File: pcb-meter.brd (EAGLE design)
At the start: 100 x 80 mm, 41 parts

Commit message: Update
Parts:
- added C3, C5, C8, C9: 100n, capacitors:C050-024X044
- added C4, C6: 10u/35V, capacitors-electrolytic:E2-5
- added HL13: BLUE(3MM), optoelectronics:LED3MM-H
- added R20: 1.5k, resistors:R-0207/10
- moved R19 623.9 mm to (34.0, 30.0), turned to 270 degrees
- moved R18 616.2 mm to (43.5, 35.0), turned to 180 degrees
- moved R17 600.3 mm to (43.5, 32.5), turned to 180 degrees
- moved R16 584.3 mm to (43.5, 30.0), turned to 180 degrees
- moved R15 577.1 mm to (56.0, 35.0), turned to 180 degrees
- moved R14 561.2 mm to (56.0, 32.5), turned to 180 degrees
- moved R13 545.3 mm to (56.0, 30.0), turned to 180 degrees
- moved R12 538.5 mm to (68.5, 35.0), turned to 180 degrees
- moved R11 522.7 mm to (68.5, 32.5), turned to 180 degrees
- moved R10 506.9 mm to (68.5, 30.0), turned to 180 degrees
- moved R9 500.6 mm to (81.0, 35.0), turned to 180 degrees
- moved R8 482.4 mm to (81.0, 30.0), turned to 180 degrees
- moved R7 471.6 mm to (81.0, 32.5), turned to 180 degrees
- moved HL12 436.4 mm to (95.5, 6.00), flipped to the bottom, turned to 180 degrees
- moved HL11 419.7 mm to (90.5, 6.00), flipped to the bottom, turned to 180 degrees
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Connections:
- removed net V+: DA1.8, DA2.3, DA3.3, DA4.3
- removed net V-: DA1.4, DA2.12, DA3.12, DA4.12
- new net N$36: DA1.6, DA1.7
- net +15V: now also C3.2, C4.+, C5.2, C8.2, C9.2, DA1.8, DA2.3, DA3.3, DA4.3
- net -15V: now also C3.1, C5.1, C6.-, C8.1, C9.1, DA1.4, DA2.12, DA3.12, DA4.12
- net GND: now also C4.-, C6.+, DA1.5, HL13.K
- net N$1: now also R20.2
- net N$11: now also DA4.4; no longer DA4.10
- net N$12: now also DA4.6; no longer DA4.8
- net N$13: now also DA4.10; no longer DA4.6
- net N$14: now also DA4.2; no longer DA4.13
- net N$15: now also DA4.1; no longer DA4.14
- net N$16: now also DA4.13; no longer DA4.1
- net N$17: now also DA4.14; no longer DA4.2
- net N$18: now also DA3.2; no longer DA3.13
- net N$19: now also DA3.1; no longer DA3.14
- net N$2: now also R1.1
- net N$20: now also DA3.13; no longer DA3.1
- net N$21: now also DA3.14; no longer DA3.2
- net N$22: now also DA2.2; no longer DA2.13
- net N$23: now also DA2.1; no longer DA2.14
- net N$24: now also DA2.13; no longer DA2.1
- net N$25: now also DA2.14; no longer DA2.2
- net N$26: now also C1.+, R3.2
- net N$27: now also DA4.8; no longer DA4.4
- net N$28: now also DA3.4; no longer DA3.10
- net N$29: now also DA3.6; no longer DA3.8
- net N$30: now also DA3.10; no longer DA3.6
- net N$31: now also DA3.8; no longer DA3.4
- net N$32: now also DA2.4; no longer DA2.10
- net N$33: now also DA2.6; no longer DA2.8
- net N$34: now also DA2.10; no longer DA2.6
- net N$35: now also DA2.8; no longer DA2.4
- net N$9: now also HL13.A, R20.1; no longer C1.+, R3.2
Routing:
- net -15V: track 0.00 -> 152.0 mm
- net +15V: track 0.00 -> 128.1 mm
- net N$1: track 0.00 -> 94.1 mm
- net N$26: track 0.00 -> 90.6 mm
- net N$14: track 0.00 -> 28.3 mm
- net N$28: track 0.00 -> 25.3 mm
- net N$5: track 0.00 -> 24.9 mm
- net N$8: track 0.00 -> 24.4 mm
- net N$34: track 0.00 -> 23.0 mm
- net N$11: track 0.00 -> 22.4 mm
- net N$16: track 0.00 -> 22.0 mm
- net N$12: track 0.00 -> 21.2 mm
- net N$33: track 0.00 -> 20.2 mm
- net N$30: track 0.00 -> 20.2 mm
- net N$13: track 0.00 -> 19.9 mm
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- added copper zone on layer 1, net GND
- added copper zone on layer 16, net GND
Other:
- board size 100 x 80 mm -> 68.5 x 35 mm

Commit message: Renumber pcb-meter
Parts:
- removed C9: 100n, capacitors:C050-024X044
- added C7: 1u/50V, capacitors-electrolytic:E1,5-4
- C1: value 1u/50V -> 10u/35V; device capacitors-electrolytic:E1,5-4 -> capacitors-electrolytic:E2-5
- C2: value 47n -> 10u/35V; device capacitors:C050-025X075 -> capacitors-electrolytic:E2-5
- C4, C6: value 10u/35V -> 100n; device capacitors-electrolytic:E2-5 -> capacitors:C050-024X044
- C8: value 100n -> 47n; device capacitors:C050-024X044 -> capacitors:C050-025X075
- HL1: value GREEN(3MM) -> BLUE(3MM)
- HL12: value RED(3MM) -> YELLOW(3MM)
- HL13: value BLUE(3MM) -> RED(3MM)
- HL9: value YELLOW(3MM) -> GREEN(3MM)
- R1: value 56k -> 1.5k
- R10: value 2.2k -> 560R
- R11: value 1.5k -> 820R
- R13: value 820R -> 1.5k
- R14: value 560R -> 2.2k
- R15: value 330R -> 3.3k
- R16: value 330R -> 12k
- R17: value 220R -> 5.6k
- R18: value 220R -> 15k
- R19: value 270R -> 1k
- R2: value 150k -> 56k
- R20: value 1.5k -> 180R
- R3: value 1.8k -> 150k
- R4: value 15k -> 1.8k
- R5: value 180R -> 270R
- R6: value 1k -> 220R
- R7: value 12k -> 220R
- R8: value 5.6k -> 330R
- R9: value 3.3k -> 330R
- moved R1 65.0 mm to (31.5, 30.0)
- moved R4 63.0 mm to (97.0, 14.0), turned to 90 degrees
- moved HL13 62.5 mm to (95.5, 6.00)
- moved C2 53.2 mm to (90.0, 31.0)
- moved C6 49.4 mm to (46.0, 8.50), turned to 0 degrees
- moved C3 40.3 mm to (81.5, 27.5), turned to 180 degrees
- moved R16 37.6 mm to (81.0, 32.5)
- moved R17 37.6 mm to (81.0, 30.0)
- moved R7 37.5 mm to (43.5, 32.5)
- moved R8 37.5 mm to (43.5, 30.0)
- moved C4 34.0 mm to (70.0, 8.50), turned to 0 degrees
- moved C8 31.9 mm to (39.0, 16.0), turned to 90 degrees
- moved R15 25.0 mm to (81.0, 35.0)
- moved R9 25.0 mm to (56.0, 35.0)
- moved DA2 24.0 mm to (70.0, 19.5)
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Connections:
- net +15V: now also C1.+, C4.2, C6.2, R17.1, R19.2, R20.2; no longer C2.2, C4.+, C9.2, R5.2, R6.2, R8.1
- net -15V: now also C2.-, C4.1, C6.1, HL13.K, R18.1; no longer C6.-, C8.1, C9.1, HL12.K, R4.1
- net GND: now also C2.+, C7.-, HL1.K, R5.2; no longer C4.-, C6.+, HL13.K, R19.2
- net N$1: now also R1.2; no longer R20.2
- net N$10: now also C8.1, R20.1; no longer C2.1, R5.1
- net N$11: now also DA2.4, R16.1, R17.2; no longer DA4.4, R7.1, R8.2
- net N$12: now also DA2.6, R15.1, R16.2; no longer DA4.6, R7.2, R9.1
- net N$13: now also DA2.10, R14.1, R15.2; no longer DA4.10, R10.1, R9.2
- net N$14: now also DA2.2, HL12.K, HL13.A; no longer DA4.2, HL11.K, HL12.A
- net N$15: now also DA2.1, HL11.K, HL12.A; no longer DA4.1, HL10.K, HL11.A
- net N$16: now also DA2.13, HL10.K, HL11.A; no longer DA4.13, HL10.A, HL9.K
- net N$17: now also DA2.14, HL10.A, HL9.K; no longer DA4.14, HL8.K, HL9.A
- net N$18: now also DA4.2, HL8.K, HL9.A; no longer DA3.2, HL7.K, HL8.A
- net N$19: now also DA4.1, HL7.K, HL8.A; no longer DA3.1, HL6.K, HL7.A
- net N$2: now also R2.1; no longer R1.1
- net N$20: now also DA4.13, HL6.K, HL7.A; no longer DA3.13, HL5.K, HL6.A
- net N$21: now also DA4.14, HL5.K, HL6.A; no longer DA3.14, HL4.K, HL5.A
- net N$22: now also DA3.2, HL4.K, HL5.A; no longer DA2.2, HL3.K, HL4.A
- net N$23: now also DA3.1, HL3.K, HL4.A; no longer DA2.1, HL2.K, HL3.A
- net N$24: now also DA3.13, HL2.K, HL3.A; no longer DA2.13, HL1.K, HL2.A
- net N$25: now also DA3.14, HL2.A; no longer DA2.14, HL1.A
- net N$26: now also C7.+, R4.2; no longer C1.+, R3.2
- net N$27: now also DA2.8, R13.1, R14.2; no longer DA4.8, R10.2, R11.1
- net N$28: now also DA4.4, R13.2; no longer DA3.4, R11.2
- net N$29: now also DA4.6, R11.1; no longer DA3.6, R13.1
- net N$30: now also DA4.10, R10.1, R11.2; no longer DA3.10, R13.2, R14.1
- net N$31: now also DA4.8, R10.2, R9.1; no longer DA3.8, R14.2, R15.1
- net N$32: now also DA3.4, R8.1, R9.2; no longer DA2.4, R15.2, R16.1
- net N$33: now also DA3.6, R7.1, R8.2; no longer DA2.6, R16.2, R17.1
- net N$34: now also DA3.10, R6.1, R7.2; no longer DA2.10, R17.2, R18.1
- net N$35: now also DA3.8, R5.1, R6.2; no longer DA2.8, R18.2, R19.1
- net N$5: now also R2.2, R3.1; no longer R1.2, R2.1
- net N$6: now also R18.2, R19.1; no longer R4.2, R6.1
- net N$8: now also R3.2, R4.1; no longer R2.2, R3.1
- net N$9: now also HL1.A, R1.1; no longer HL13.A, R20.1

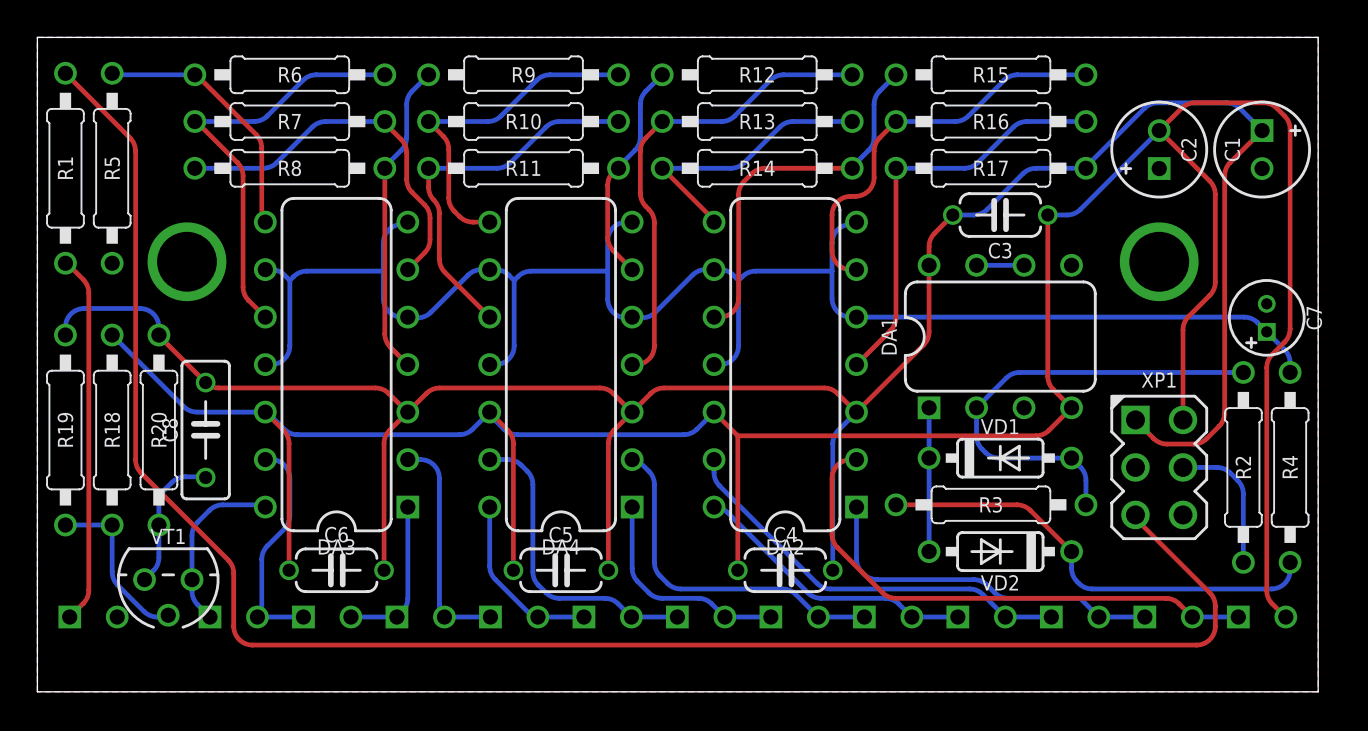
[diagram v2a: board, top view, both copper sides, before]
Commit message: Remove PP indicator
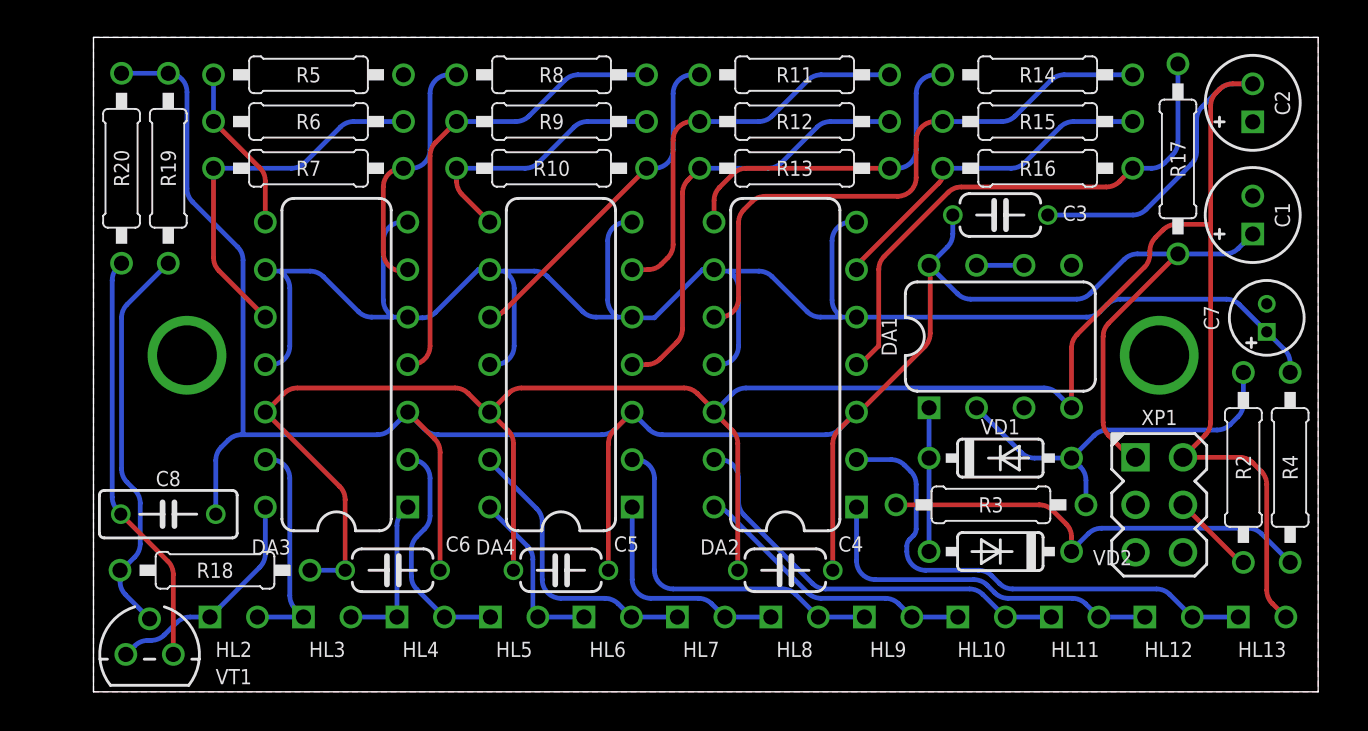
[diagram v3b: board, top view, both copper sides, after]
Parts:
- removed HL1: BLUE(3MM), optoelectronics:LED3MM-H
- removed R1: 1.5k, resistors:R-0207/10
- moved R14 15.8 mm to (83.5, 35.0)
- moved R11 15.3 mm to (70.5, 35.0)
- moved R19 15.0 mm to (37.0, 30.0)
- moved R8 14.9 mm to (57.5, 35.0)
- moved R20 14.1 mm to (34.5, 30.0)
- moved R5 11.6 mm to (44.5, 35.0), turned to 0 degrees
- moved R17 10.0 mm to (91.0, 30.5), turned to 90 degrees
- moved R18 9.30 mm to (39.5, 8.50), turned to 180 degrees
- moved C2 5.59 mm to (95.0, 33.5)
- moved C8 4.92 mm to (37.0, 11.5), turned to 0 degrees
- moved VT1 4.12 mm to (36.0, 4.00), turned to 0 degrees
- moved C1 3.54 mm to (95.0, 27.5), turned to 90 degrees
- moved R15 3.54 mm to (83.5, 32.5)
- moved R16 3.54 mm to (83.5, 30.0)
- moved R12 3.20 mm to (70.5, 32.5)
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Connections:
- removed net N$1: R1.2, XP1.5
- removed net N$9: HL1.A, R1.1
- net GND: no longer HL1.K
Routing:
- net N$1: track 94.1 -> 0.00 mm
- net N$9: track 19.8 -> 0.00 mm
- net N$10: track 7.56 -> 22.3 mm
- net -15V: track 152.0 -> 139.7 mm
- net N$6: track 9.16 -> 21.3 mm
- net N$13: track 19.9 -> 31.3 mm
- net N$29: track 12.0 -> 21.3 mm
- net N$32: track 16.8 -> 25.2 mm
- net +15V: track 128.1 -> 135.6 mm
- net N$26: track 90.6 -> 97.5 mm
- net N$33: track 20.2 -> 13.4 mm
- net N$11: track 22.4 -> 28.9 mm
- net N$35: track 13.9 -> 8.96 mm
- net N$5: track 24.9 -> 21.0 mm
- net N$31: track 18.4 -> 14.6 mm
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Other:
- board size 68.5 x 35 mm -> 65.5 x 35 mm

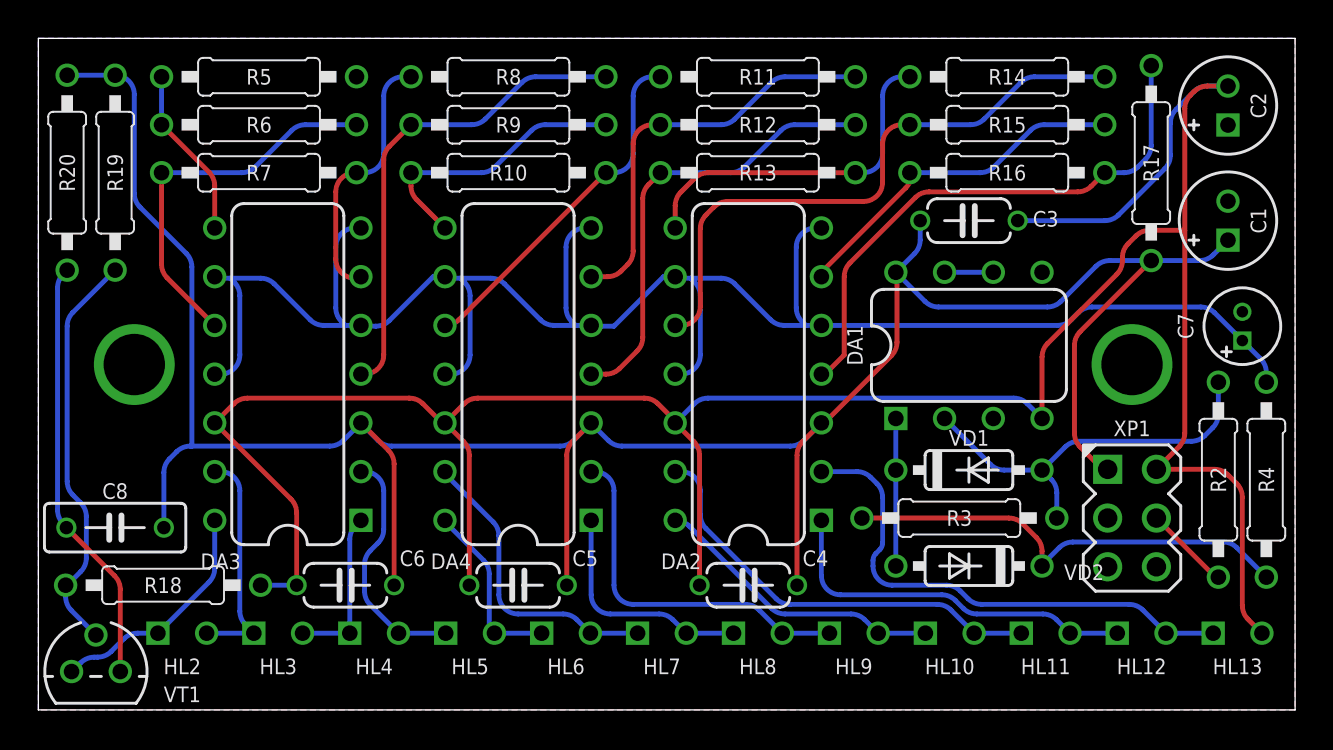
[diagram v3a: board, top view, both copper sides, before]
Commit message: Round pcb edges for pcb-meter
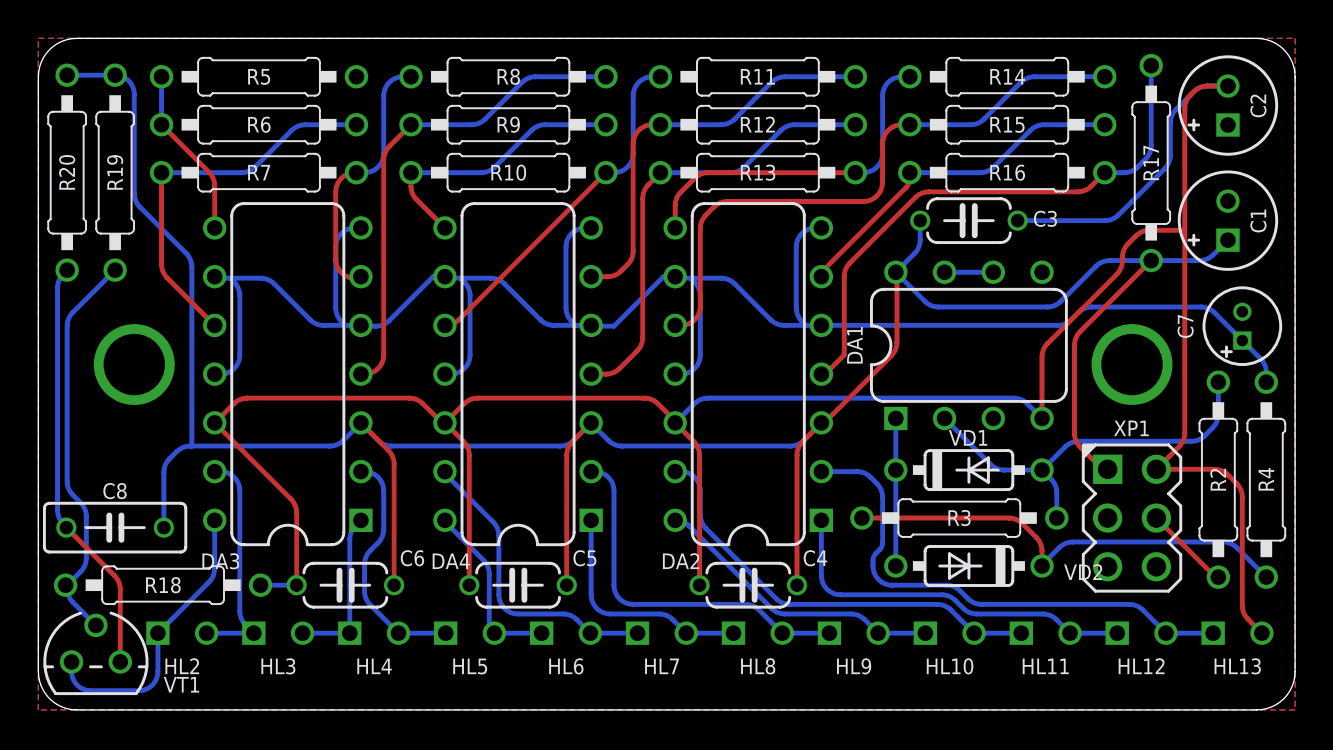
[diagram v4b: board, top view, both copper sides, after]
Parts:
- moved VT1 0.50 mm to (36.0, 4.50)
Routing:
- net N$25: track 12.2 -> 14.9 mm
- net N$6: track 21.3 -> 20.8 mm
- net N$10: track 22.3 -> 21.8 mm
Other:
- outline, holes or cut-outs redrawn
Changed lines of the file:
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@@
 <layers>
 <layer number="1" name="Top" color="4" fill="1" visible="yes" active="yes"/>
-<layer number="16" name="Bottom" color="1" fill="1" visible="no" active="yes"/>
+<layer number="16" name="Bottom" color="1" fill="1" visible="yes" active="yes"/>
 <layer number="17" name="Pads" color="2" fill="1" visible="yes" active="yes"/>
 <layer number="18" name="Vias" color="2" fill="1" visible="yes" active="yes"/>
@@
 <board>
 <plain>
-<wire x1="33" y1="2" x2="98.5" y2="2" width="0" layer="20"/>
-<wire x1="98.5" y1="2" x2="98.5" y2="37" width="0" layer="20"/>
-<wire x1="98.5" y1="37" x2="33" y2="37" width="0" layer="20"/>
-<wire x1="33" y1="37" x2="33" y2="2" width="0" layer="20"/>
+<wire x1="33" y1="35" x2="33" y2="4" width="0" layer="20"/>
+<wire x1="33" y1="4" x2="35" y2="2" width="0" layer="20" curve="90"/>
+<wire x1="35" y1="2" x2="96.5" y2="2" width="0" layer="20"/>
+<wire x1="96.5" y1="2" x2="98.5" y2="4" width="0" layer="20" curve="90"/>
+<wire x1="98.5" y1="4" x2="98.5" y2="35" width="0" layer="20"/>
+<wire x1="98.5" y1="35" x2="96.5" y2="37" width="0" layer="20" curve="90"/>
+<wire x1="96.5" y1="37" x2="35" y2="37" width="0" layer="20"/>
+<wire x1="35" y1="37" x2="33" y2="35" width="0" layer="20" curve="90"/>
 </plain>
 <attributes>
@@
 <attribute name="NAME" x="66.5" y="9.34" size="0.8128" layer="25" ratio="15" align="bottom-center"/>
 </element>
-<element name="VT1" library="transistors-pnp" package="TO92" value="BC556" x="36" y="4" smashed="yes">
-<attribute name="NAME" x="40.5" y="2.405" size="0.8128" layer="25" ratio="15" align="bottom-center"/>
+<element name="VT1" library="transistors-pnp" package="TO92" value="BC556" x="36" y="4.5" smashed="yes">
+<attribute name="NAME" x="40.5" y="2.905" size="0.8128" layer="25" ratio="15" align="bottom-center"/>
 </element>
 <element name="R18" library="resistors" package="R-0207/10" value="15k" x="39.5" y="8.5" rot="R180"/>
@@
 <contactref element="VT1" pad="2"/>
 <contactref element="R19" pad="1"/>
-<wire x1="34.42" y1="8.5" x2="34.42" y2="7.8992125" width="0.254" layer="16"/>
-<wire x1="34.42" y1="7.8992125" x2="34.71289375" y2="7.19210625" width="0.254" layer="16" curve="45"/>
-<wire x1="34.71289375" y1="7.19210625" x2="36" y2="5.905" width="0.254" layer="16"/>
 <wire x1="34.42" y1="8.5" x2="34.5" y2="8.5" width="0.254" layer="16"/>
 <wire x1="34.5" y1="8.5" x2="35.20710625" y2="9.20710625" width="0.254" layer="16"/>
@@
 <wire x1="34.5" y1="22.0057875" x2="34.79289375" y2="22.71289375" width="0.254" layer="16" curve="-45"/>
 <wire x1="34.79289375" y1="22.71289375" x2="37" y2="24.92" width="0.254" layer="16"/>
+<wire x1="34.5" y1="8.5" x2="34.5" y2="8.3192125" width="0.254" layer="16"/>
+<wire x1="34.5" y1="8.3192125" x2="34.79289375" y2="7.61210625" width="0.254" layer="16" curve="45"/>
+<wire x1="34.79289375" y1="7.61210625" x2="36" y2="6.405" width="0.254" layer="16"/>
 </signal>
 <signal name="N$10">
@@
 <contactref element="R20" pad="1"/>
 <contactref element="C8" pad="1"/>
-<wire x1="37.27" y1="4" x2="37.27" y2="8.2757875" width="0.254" layer="1"/>
+<wire x1="37.27" y1="4.5" x2="37.27" y2="8.2757875" width="0.254" layer="1"/>
 <wire x1="37.27" y1="8.2757875" x2="36.97710625" y2="8.98289375" width="0.254" layer="1" curve="45"/>
 <wire x1="36.97710625" y1="8.98289375" x2="34.46" y2="11.5" width="0.254" layer="1"/>
@@
 <contactref element="VT1" pad="1"/>
 <contactref element="DA3" pad="14"/>
-<wire x1="34.73" y1="4" x2="34.75" y2="4" width="0.254" layer="16"/>
-<wire x1="34.75" y1="4" x2="35.20710625" y2="4.45710625" width="0.254" layer="16"/>
-<wire x1="35.20710625" y1="4.45710625" x2="35.9142125" y2="4.75" width="0.254" layer="16" curve="-45"/>
-<wire x1="35.9142125" y1="4.75" x2="36.0857875" y2="4.75" width="0.254" layer="16"/>
-<wire x1="36.0857875" y1="4.75" x2="36.79289375" y2="5.04289375" width="0.254" layer="16" curve="45"/>
-<wire x1="36.79289375" y1="5.04289375" x2="37.45710625" y2="5.70710625" width="0.254" layer="16"/>
-<wire x1="37.45710625" y1="5.70710625" x2="38.1642125" y2="6" width="0.254" layer="16" curve="-45"/>
-<wire x1="38.1642125" y1="6" x2="39.23" y2="6" width="0.254" layer="16"/>
 <wire x1="42.19" y1="11.88" x2="42.19" y2="9.3742125" width="0.254" layer="16"/>
 <wire x1="42.19" y1="9.3742125" x2="41.89710625" y2="8.66710625" width="0.254" layer="16" curve="-45"/>
 <wire x1="41.89710625" y1="8.66710625" x2="39.23" y2="6" width="0.254" layer="16"/>
+<wire x1="34.73" y1="4.5" x2="34.73" y2="4" width="0.254" layer="16"/>
+<wire x1="34.73" y1="4" x2="35.73" y2="3" width="0.254" layer="16" curve="90"/>
+<wire x1="39.23" y1="6" x2="39.23" y2="4" width="0.254" layer="16"/>
+<wire x1="39.23" y1="4" x2="38.23" y2="3" width="0.254" layer="16" curve="-90"/>
+<wire x1="38.23" y1="3" x2="35.73" y2="3" width="0.254" layer="16"/>
 </signal>
 <signal name="N$26">
